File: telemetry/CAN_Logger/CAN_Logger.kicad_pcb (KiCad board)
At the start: 2 copper layers, 109.3 x 58.3 mm, 19 parts, among them U101 TPS560430YF

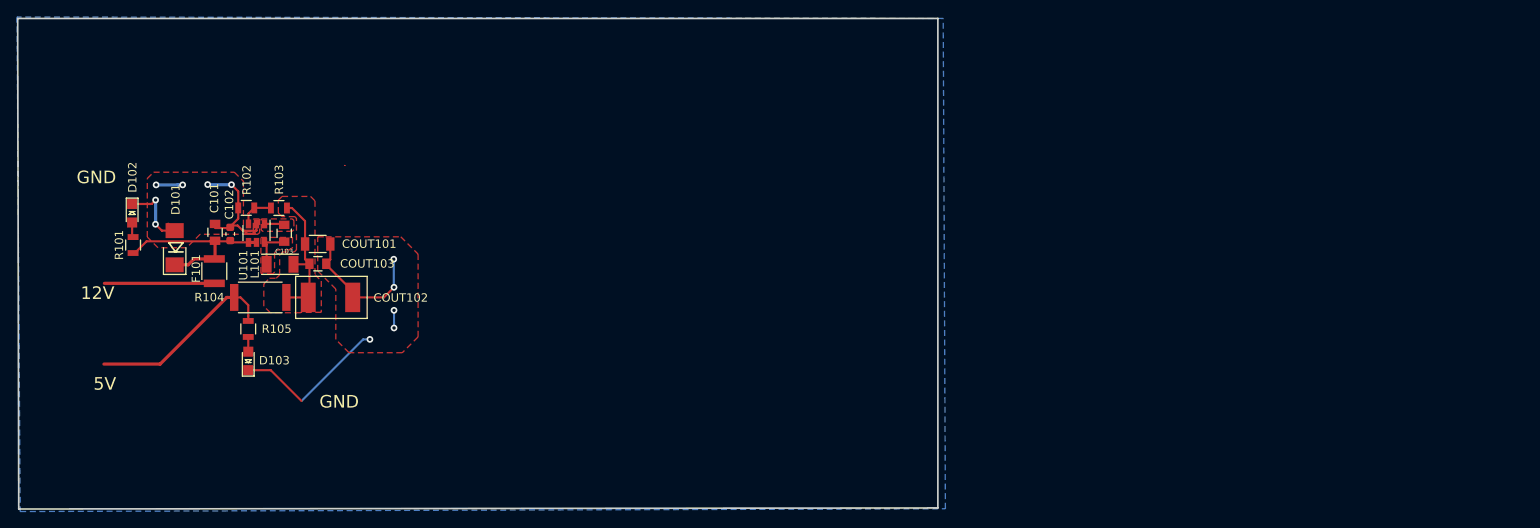
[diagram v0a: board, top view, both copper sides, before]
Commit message: Began PCB layout, and schematic layout boxing
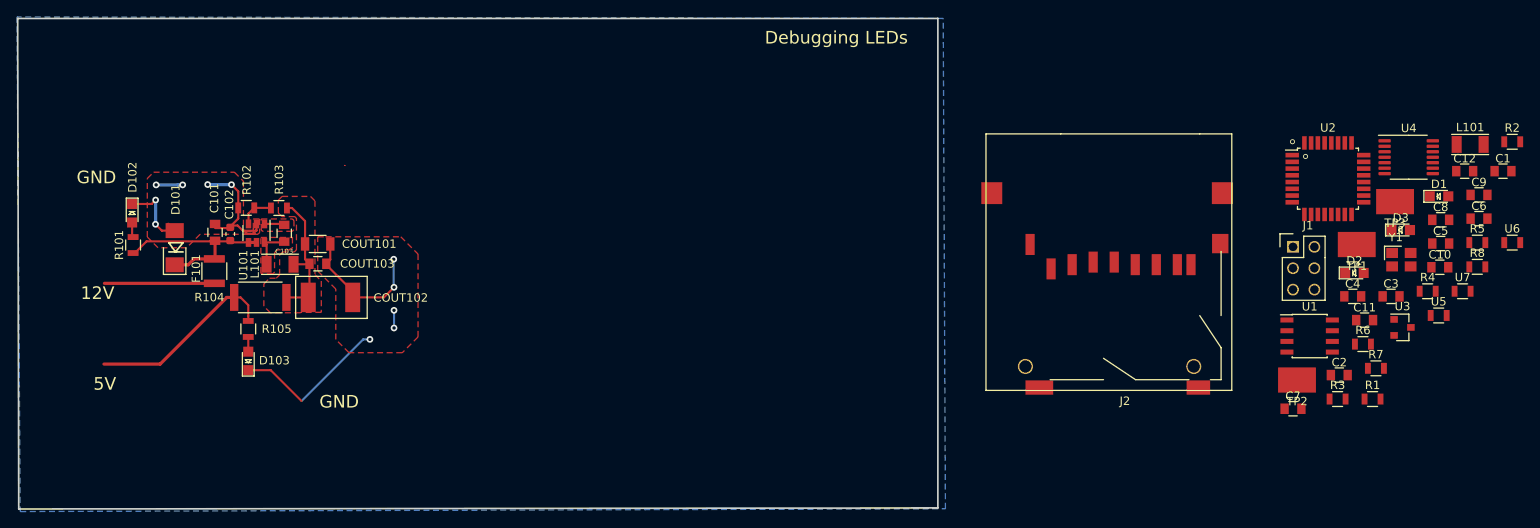
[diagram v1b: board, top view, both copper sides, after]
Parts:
- added C1: C_0.1uF, footprints:C_0805_OEM, F.Cu at (274.8, 94.6)
- added C10: C_10uF, footprints:C_0805_OEM, F.Cu at (267.3, 106.0)
- added C11: C_1uF, footprints:C_0805_OEM, F.Cu at (258.4, 112.3)
- added C12: C_0.1uF, footprints:C_0805_OEM, F.Cu at (270.2, 94.6)
- added C2: C_0.1uF, footprints:C_0805_OEM, F.Cu at (255.3, 118.8)
- added C3: C_100pF, footprints:C_0805_OEM, F.Cu at (261.5, 109.5)
- added C4: C_30pF, footprints:C_0805_OEM, F.Cu at (256.9, 109.5)
- added C5: C_30pF, footprints:C_0805_OEM, F.Cu at (267.4, 103.2)
- added C6: C_0.1uF, footprints:C_0805_OEM, F.Cu at (271.9, 100.2)
- added C7: C_0.1uF, footprints:C_0805_OEM, F.Cu at (249.8, 122.8)
- added C8: C_0.1uF, footprints:C_0805_OEM, F.Cu at (267.4, 100.4)
- added C9: C_0.1uF, footprints:C_0805_OEM, F.Cu at (271.9, 97.4)
- added D1: LED_0805, footprints:LED_0805_OEM, F.Cu at (267.2, 97.6)
- added D2: LED_0805, footprints:LED_0805_OEM, F.Cu at (257.1, 106.7)
- added D3: LED_0805, footprints:LED_0805_OEM, F.Cu at (262.6, 101.6)
- added J1: CONN_02X03, footprints:Pin_Header_Straight_2x03, F.Cu at (249.8, 103.6)
- added J2: SD_socket, footprints:sd_socket_molex_5009980900, F.Cu at (228.6, 105.4)
- added L101: L_100uH, footprints:L_100uH_OEM, F.Cu at (270.9, 91.4)
- added R1: R_200, footprints:R_0805_OEM, F.Cu at (259.3, 121.7)
- added R2: R_200, footprints:R_0805_OEM, F.Cu at (275.9, 91.1)
- added R3: R_200, footprints:R_0805_OEM, F.Cu at (255.1, 121.7)
- added R4: R_120_DNP, footprints:R_0805_OEM, F.Cu at (265.8, 108.9)
- added R5: R_10K, footprints:R_0805_OEM, F.Cu at (271.7, 103.1)
- added R6: R_10K, footprints:R_0805_OEM, F.Cu at (258.2, 115.2)
- added R7: R_10K, footprints:R_0805_OEM, F.Cu at (259.7, 118.0)
- added R8: R_100, footprints:R_0805_OEM, F.Cu at (271.7, 106.0)
- added TP1: Test_Point_SMD, footprints:Test_Point_SMD, F.Cu at (257.4, 103.3)
- added TP2: Test_Point_SMD, footprints:Test_Point_SMD, F.Cu at (250.3, 119.4)
- added TP3: Test_Point_SMD, footprints:Test_Point_SMD, F.Cu at (262.0, 98.2)
- added U1: MCP2561-E_SN, footprints:SOIC-8_3.9x4.9mm_Pitch1.27mm_OEM, F.Cu at (251.8, 114.2)
- added U2: ATMEGA16M1, footprints:TQFP-32_7x7mm_Pitch0.8mm, F.Cu at (254.0, 95.5)
- added U3: LM3480, Package_TO_SOT_SMD:SOT-23, F.Cu at (262.9, 113.2)
- added U4: TXB0104, Package_SO:TSSOP-14_4.4x5mm_P0.65mm, F.Cu at (263.6, 92.9)
- added U5: R_500, footprints:R_0805_OEM, F.Cu at (267.2, 111.8)
- added U6: R_500, footprints:R_0805_OEM, F.Cu at (275.9, 103.1)
- added U7: R_500, footprints:R_0805_OEM, F.Cu at (270.0, 108.9)
- added Y1: Crystal_SMD, footprints:Crystal_SMD_FA238, F.Cu at (262.7, 105.1)
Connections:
- net VCC renamed +5V
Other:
- board text added: "Debugging LEDs"
